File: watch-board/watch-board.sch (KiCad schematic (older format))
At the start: 41 parts

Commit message: finished LTC3531-3 design
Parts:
- removed BT?: BAT_ML2020, symbol luke:BAT_ML2020
- removed C?: C_10uF, Capacitor_SMD:C_0805_2012Metric, symbol luke:C_10uF
- removed C? (x2): C_1uF, footprints:C_0805_OEM, symbol formula:C_1uF
- removed R? (x2): R_1M, Resistor_SMD:R_0805_2012Metric, symbol luke:R_1M
- removed R?: R_475K, Resistor_SMD:R_0805_2012Metric, symbol luke:R_475K
- removed R?: R_2K, Resistor_SMD:R_0805_2012Metric, symbol luke:R_2K
- removed R?: R_165K, Resistor_SMD:R_0805_2012Metric, symbol luke:R_165K
- removed R?: R_499K, Resistor_SMD:R_0805_2012Metric, symbol luke:R_499K
- removed R?: R_160, Resistor_SMD:R_0805_2012Metric, symbol luke:R_160
- removed SC?: Solar-Cells_KXOB25-05X3F, symbol luke:Solar-Cells_KXOB25-05X3F
- removed U?: Regulator_LTC3105, Digikey-footprints:MSOP-12-1EP_W3mm, symbol luke:Regulator_LTC3105
- added BT?: BAT_ML2020, symbol luke:BAT_ML2020
- added C?: C_10uF, Capacitor_SMD:C_0805_2012Metric, symbol luke:C_10uF
- added C?: C_2.2uF, Capacitor_SMD:C_0805_2012Metric, symbol luke:C_2.2uF
- added L?: L_22uH, Inductor_SMD:L_Wuerth_WE-TPC-3816, symbol luke:L_22uH
- added L?: L_10uH, Inductor_SMD:L_1812_4532Metric, symbol luke:L_10uH
- added SC?: Solar-Cells_KXOB25-05X3F, symbol luke:Solar-Cells_KXOB25-05X3F
- added U?: Regulator_BQ25504, Package_DFN_QFN:QFN-16-1EP_3x3mm_P0.5mm_EP1.8x1.8mm, symbol luke:Regulator_BQ25504
- added U?: Regulator_LTC3531-3, Package_TO_SOT_SMD:TSOT-23-6, symbol luke:Regulator_LTC3531-3
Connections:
- wire segments 121 -> 118

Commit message: finished REV1 of board
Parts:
- removed BT? (x2): BAT_ML2020, symbol luke:BAT_ML2020
- removed C?: C_4.7uF, Capacitor_SMD:C_1206_3216Metric, symbol luke:C_4.7uF
- removed C?: C_7pF, Capacitor_SMD:C_0805_2012Metric, symbol luke:C_7pF
- removed C?: C_1uF, Capacitor_SMD:C_0805_2012Metric, symbol luke:C_1uF
- removed C?: C_0.1uF, Capacitor_SMD:C_0805_2012Metric, symbol luke:C_0.1uF
- removed D? (x3): D-Schotkey_BAT54HT1G, Diode_SMD:D_SOD-323, symbol luke:D-Schotkey_BAT54HT1G
- removed Q?: Transistor_FZT796ATA, Package_TO_SOT_SMD:SOT-223, symbol luke:Transistor_FZT796ATA
- removed R?: R_51.1K, Resistor_SMD:R_0805_2012Metric, symbol luke:R_51.1K
- removed R?: R_78.7K, Resistor_SMD:R_0805_2012Metric, symbol luke:R_78.7K
- removed R?: R_160, Resistor_SMD:R_0805_2012Metric, symbol luke:R_160
- removed R?: R_100K, Resistor_SMD:R_0805_2012Metric, symbol luke:R_100K
- removed R?: R_200K, Resistor_SMD:R_0805_2012Metric, symbol luke:R_200K
- removed R?: R_1.2M, Resistor_SMD:R_0805_2012Metric, symbol luke:R_1.2M
- removed R?: R_49.9K, Resistor_SMD:R_0805_2012Metric, symbol luke:R_49.9K
- removed SC?: Solar-Cells_KXOB25-02X8F, symbol luke:Solar-Cells_KXOB25-02X8F
- removed U?: Comparitor_TPS3700DDCR, digikey-footprints:SOT-23-6, symbol luke:Comparitor_TPS3700DDCR
- removed U?: Regulator_LP2980-ADJ, Package_TO_SOT_SMD:SOT-23-5, symbol luke:Regulator_LP2980-ADJ
- added BT1: BAT_ML1220, Battery:Battery_Panasonic_CR1220-VCN_Vertical_CircularHoles, symbol luke:BAT_ML1220
- added C10: C_2.2uF, Capacitor_SMD:C_0805_2012Metric, symbol luke:C_2.2uF
- added C11, C17: C_0.1uF, Capacitor_SMD:C_0805_2012Metric, symbol luke:C_0.1uF
- added C13: C_0.01uF, Capacitor_SMD:C_0805_2012Metric, symbol luke:C_0.01uF
- added C14, C16: C_4.7uF, Capacitor_SMD:C_0805_2012Metric, symbol luke:C_4.7uF
- added C7, C9: C_20pF, Capacitor_SMD:C_0805_2012Metric, symbol luke:C_20pF
- added D1: D-Schotkey_BAT54HT1G, Diode_SMD:D_SOD-323, symbol luke:D-Schotkey_BAT54HT1G
- added J2: Conn_02x05, Connector_PinSocket_2.54mm:PinSocket_2x05_P2.54mm_Vertical, symbol luke:Conn_02x05
- added J3: FPC-Conn_01x08, luke-footprints:Connector_Molex-5014610891, symbol luke:FPC-Conn_01x08
- added R1: R_330, footprints:R_0805_OEM, symbol luke:R_330
- added R10, R7: R_4.22M, Resistor_SMD:R_0805_2012Metric, symbol luke:R_4.22M
- added R11: R_5.11M, Resistor_SMD:R_0805_2012Metric, symbol luke:R_5.11M
- added R12: R_6.04M, Resistor_SMD:R_0805_2012Metric, symbol luke:R_6.04M
- added R13: R_10M, Resistor_SMD:R_0805_2012Metric, symbol luke:R_10M
- added R14: R_3.83M, Resistor_SMD:R_0805_2012Metric, symbol luke:R_3.83M
- added R2: R_220K, Resistor_SMD:R_0805_2012Metric, symbol luke:R_220K
- added R3, R4: R_10K, Resistor_SMD:R_0805_2012Metric, symbol luke:R_10K
- added R5: R_3.74M, Resistor_SMD:R_0805_2012Metric, symbol luke:R_3.74M
- added R6: R_6.19M, Resistor_SMD:R_0805_2012Metric, symbol luke:R_6.19M
- added R8: R_5.62M, Resistor_SMD:R_0805_2012Metric, symbol luke:R_5.62M
- added R9: R_806K, Resistor_SMD:R_0805_2012Metric, symbol luke:R_806K
- added S1: Switch_1767, Connector_PinSocket_2.54mm:PinSocket_1x02_P2.54mm_Vertical, symbol luke:Switch_1767
- added XTAL1: Crystals_32.768-SMD, Digikey-footprints:SMD-2_3.2x1.5mm, symbol luke:Crystals_32.768-SMD
- C1, C3, C5, C8: renamed from C?; Digi-Key_PN 399-1177-1-ND -> 399-8000-1-ND; Purchasing Link https://www.digikey.com/product-detail/en/kemet/C0805C104Z5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 -> https://www.digikey.com/product-detail/en/kemet/C0805C104M3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
- L1: renamed from L?; Purchasing Link (none) -> https://www.digikey.com/product-detail/en/murata-electronic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
- L2: renamed from L?; Purchasing Link (none) -> https://www.digikey.com/product-detail/en/w%C3%BCrth-elektr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; PurchasingLink https://www.digikey.com/product-detail/en/w%C3%BCrth-elektr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 -> (none)
- SC1: renamed from SC?; footprint (none) -> luke-footprints:Solar-Cells_KXOB25
- U3: renamed from U?; footprint Package_DFN_QFN:QFN-16-1EP_3x3mm_P0.5mm_EP1.8x1.8mm -> Package_DFN_QFN:VQFN-16-1EP_3x3mm_P0.5mm_EP1.8x1.8mm_ThermalVias
- gave numbers to parts that had none: 8
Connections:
- net labels added: BUTTON, DISP, EXTCOMIN, LOAD, MISO, MOSI, NSS, OK_HYST, OK_PROG, PA2, PA3, SCK, VBAT_OK, VBAT_OV, VBAT_UV
- net labels removed: VCC, V_BAT, V_Charge, V_Charge_ON
- wire segments 118 -> 140
- no-connect marks 0 -> 14
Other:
- note added: "Buck/Boost Converter"
- note added: "Connectors"
- note added: "Engery Harvesting"
- note added: "LCD Connector"
- note added: "R_OC"
- note added: "R_OK"
- note added: "R_OV"
- note added: "R_UV"
- note added: "STM32"
- note added: "Shake Switch"
- note removed: "Calcular ESR is 886Ohms\n160Ohm resistor used for current limiting durring charging"
- note removed: "Rt = 1500000 (high value for low current draw)\nR3 = (Rt/Vo)*Vi\nR2 = ((Rt/Vu)*(Vi-Vhys))-R3\nR1 = Rt - R2 - R3\nVi = 0.4V\nVo = 3V\nVu = 2V\nVhys = 5.5mV [(Vi+) - (Vi-)]\n\nR2 =95875 (rounding up to 100K for convience)\nR3 = 200K"
- note removed: "TODO: Add SPI Pins"
- note removed: "Vout = Vref + (Vref * (Radj/51.1K))\nVref Typical = 1.225 (min = 1.213 max = 1.237)\nRadj = 78.7K\nVout =3.11\n3.08 < Vout < 3.14"
- note removed: "use BUCK-BOOST (TPS6305) to set VDD to 3V"
- moved on the sheet: C1, C12, C15, C2, C3, C4, C5, C6, C8, J1, L1, L2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

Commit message: Schematic for Version 2
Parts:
- removed C15: C_10uF, Capacitor_SMD:C_0805_2012Metric, symbol luke:C_10uF
- removed L1: L_10uH, Inductor_SMD:L_1812_4532Metric, symbol luke:L_10uH
- removed R1: R_330, footprints:R_0805_OEM, symbol luke:R_330
- removed R10, R7: R_4.22M, Resistor_SMD:R_0805_2012Metric, symbol luke:R_4.22M
- removed R11: R_5.11M, Resistor_SMD:R_0805_2012Metric, symbol luke:R_5.11M
- removed R12: R_6.04M, Resistor_SMD:R_0805_2012Metric, symbol luke:R_6.04M
- removed R13: R_10M, Resistor_SMD:R_0805_2012Metric, symbol luke:R_10M
- removed R14: R_3.83M, Resistor_SMD:R_0805_2012Metric, symbol luke:R_3.83M
- removed R5: R_3.74M, Resistor_SMD:R_0805_2012Metric, symbol luke:R_3.74M
- removed R6: R_6.19M, Resistor_SMD:R_0805_2012Metric, symbol luke:R_6.19M
- removed U3: Regulator_BQ25504, Package_DFN_QFN:VQFN-16-1EP_3x3mm_P0.5mm_EP1.8x1.8mm_ThermalVias, symbol luke:Regulator_BQ25504
- added C33: C_10uF, Capacitor_SMD:C_0805_2012Metric, symbol luke:C_10uF
- added L3: L_10uH, Inductor_SMD:L_1812_4532Metric, symbol luke:L_10uH
- added R13: R_330, footprints:R_0805_OEM, symbol luke:R_330
- added R17: R_3.74M, Resistor_SMD:R_0805_2012Metric, symbol luke:R_3.74M
- added R18: R_6.19M, Resistor_SMD:R_0805_2012Metric, symbol luke:R_6.19M
- added R19, R22: R_4.22M, Resistor_SMD:R_0805_2012Metric, symbol luke:R_4.22M
- added R23: R_5.11M, Resistor_SMD:R_0805_2012Metric, symbol luke:R_5.11M
- added R24: R_6.04M, Resistor_SMD:R_0805_2012Metric, symbol luke:R_6.04M
- added R25: R_10M, Resistor_SMD:R_0805_2012Metric, symbol luke:R_10M
- added R26: R_3.83M, Resistor_SMD:R_0805_2012Metric, symbol luke:R_3.83M
- added U11: Regulator_BQ25504, Package_DFN_QFN:VQFN-16-1EP_3x3mm_P0.5mm_EP1.8x1.8mm_ThermalVias, symbol luke:Regulator_BQ25504
- renumbered BT1 to BT2, C1 to C19, C2 to C20, C3 to C21, C4 to C22, C5 to C23, C6 to C24, C7 to C25, C8 to C26, C9 to C27, C10 to C28, C11 to C29, C12 to C30, C13 to C31, C14 to C32, C16 to C34, C17 to C35, D1 to D2, J1 to J2, J2 to J3, J3 to J4, L2 to L4, R2 to R14, R3 to R15, R4 to R16, R8 to R20, R9 to R21, S1 to S3, SC1 to SC2, U2 to U10, U1 to U9, XTAL1 to XTAL2

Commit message: Stopping work on Watch-V2. Changing driver & Display on Watch-V1.
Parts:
- removed C28: C_2.2uF, Capacitor_SMD:C_0805_2012Metric, symbol luke:C_2.2uF
- removed C29: C_0.1uF, Capacitor_SMD:C_0805_2012Metric, symbol luke:C_0.1uF
- removed J3: Conn_02x05, Connector_PinSocket_2.54mm:PinSocket_2x05_P2.54mm_Vertical, symbol luke:Conn_02x05
- removed J4: FPC-Conn_01x08, luke-footprints:Connector_Molex-5014610891, symbol luke:FPC-Conn_01x08
- removed R15, R16: R_10K, Resistor_SMD:R_0805_2012Metric, symbol luke:R_10K
- removed U9: MCU_STM32L051K8Tx, Package_QFP:LQFP-32_7x7mm_P0.8mm, symbol luke:MCU_STM32L051K8Tx
- added BZ1: Buzzer_PB9.9-3V, symbol luke:Buzzer_PB9.9-3V
- added C10, C11, C12, C15: C_0.1uF, Capacitor_SMD:C_0805_2012Metric, symbol luke:C_0.1uF
- added C13: C_22uF, Capacitor_SMD:C_0805_2012Metric, symbol luke:C_22uF
- added C14: C_10uF, Capacitor_SMD:C_0805_2012Metric, symbol luke:C_10uF
- added R1, R2: R_4.7K, Resistor_SMD:R_0805_2012Metric, symbol luke:R_4.7K
- added R3: R_330, footprints:R_0805_OEM, symbol luke:R_330
- added R8: R_49.9K, Resistor_SMD:R_0805_2012Metric, symbol luke:R_49.9K
- added U1: LCD_OD-204, luke-footprints:LCD_OD-204, symbol luke:LCD_OD-204
- added U2: Display-Driver_PCA8561ANH, Package_DFN_QFN:QFN-32-1EP_5x5mm_P0.5mm_EP3.6x3.6mm, symbol luke:Display-Driver_PCA8561ANH
- added U3: MCU_STM32L051K8Ux, Package_DFN_QFN:QFN-32-1EP_5x5mm_P0.5mm_EP3.3x3.3mm, symbol luke:MCU_STM32L051K8Ux
- added U4: Sensor_VCNL4010, luke-footprints:Sensor_VCNL4010, symbol luke:Sensor_VCNL4010
- BT1: renamed from BT2; footprint Battery:Battery_Panasonic_CR1220-VCN_Vertical_CircularHoles -> luke-footprints:BAT_ML1220-F1A; Purchasing Link https://www.digikey.com/product-detail/en/panasonic-bsg/ML-1220-F1BN/P663-ND/2404068 -> https://www.digikey.com/product-detail/en/panasonic-bsg/ML-1220-F1AN/P295-ND/447504
- renumbered C19 to C1, C31 to C16, C32 to C17, C30 to C18, C33 to C19, C20 to C2, C34 to C20, C35 to C21, C21 to C3, C22 to C4, C23 to C5, C24 to C6, C25 to C7, C26 to C8, C27 to C9, D2 to D1, J2 to J1, L4 to L1, L3 to L2, R18 to R10, R19 to R11, R20 to R12, R21 to R13, R22 to R14, R23 to R15, R24 to R16, R25 to R17, R26 to R18, R13 to R4, R14 to R5, R17 to R9, S3 to S1, SC2 to SC1, U11 to U5, U10 to U6, XTAL2 to XTAL1
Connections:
- net labels added: 1A, 1B, 1C, 1D, 1E, 1F, 1G, 2A, 2B, 2C, 2D, 2E, 2F, 2G, BUZZER, COM1, COM2, INT, RESET, SCL, SDA, VCC
- net labels removed: EXTCOMIN, MISO, MOSI, NSS, PA2, PA3, SCK
- wire segments 140 -> 191
- no-connect marks 14 -> 25
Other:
- note added: "Conn"
- note added: "Display & Driver"
- note removed: "Connectors"
- note removed: "LCD Connector"
- moved on the sheet: BT1, C1, C16, C17, C18, C19, C2, C20, C21, C3, C4, C5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

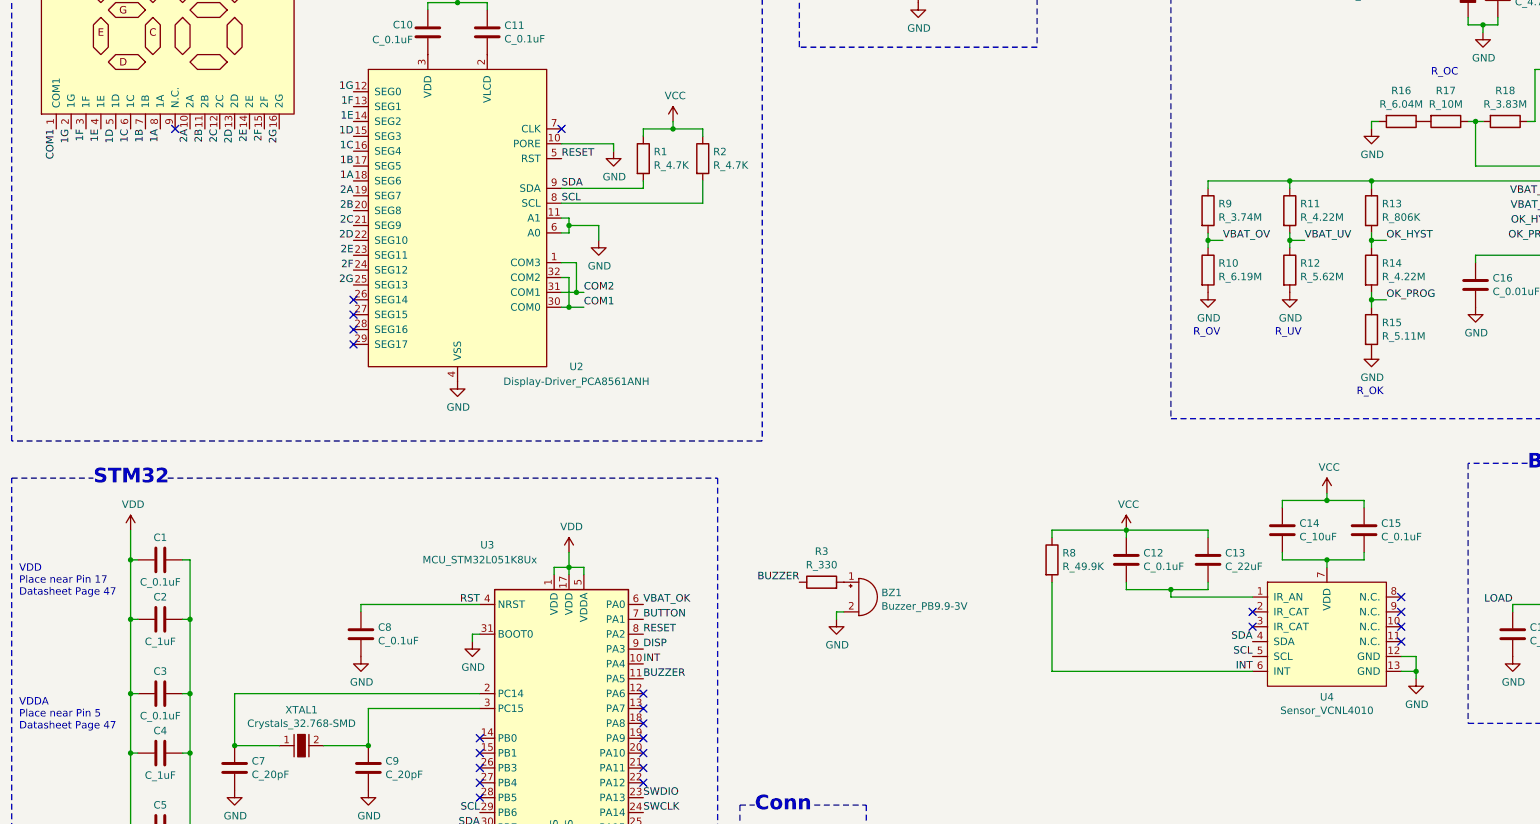
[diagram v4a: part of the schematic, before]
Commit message: Adding Phototransistors for Gesture Sensing
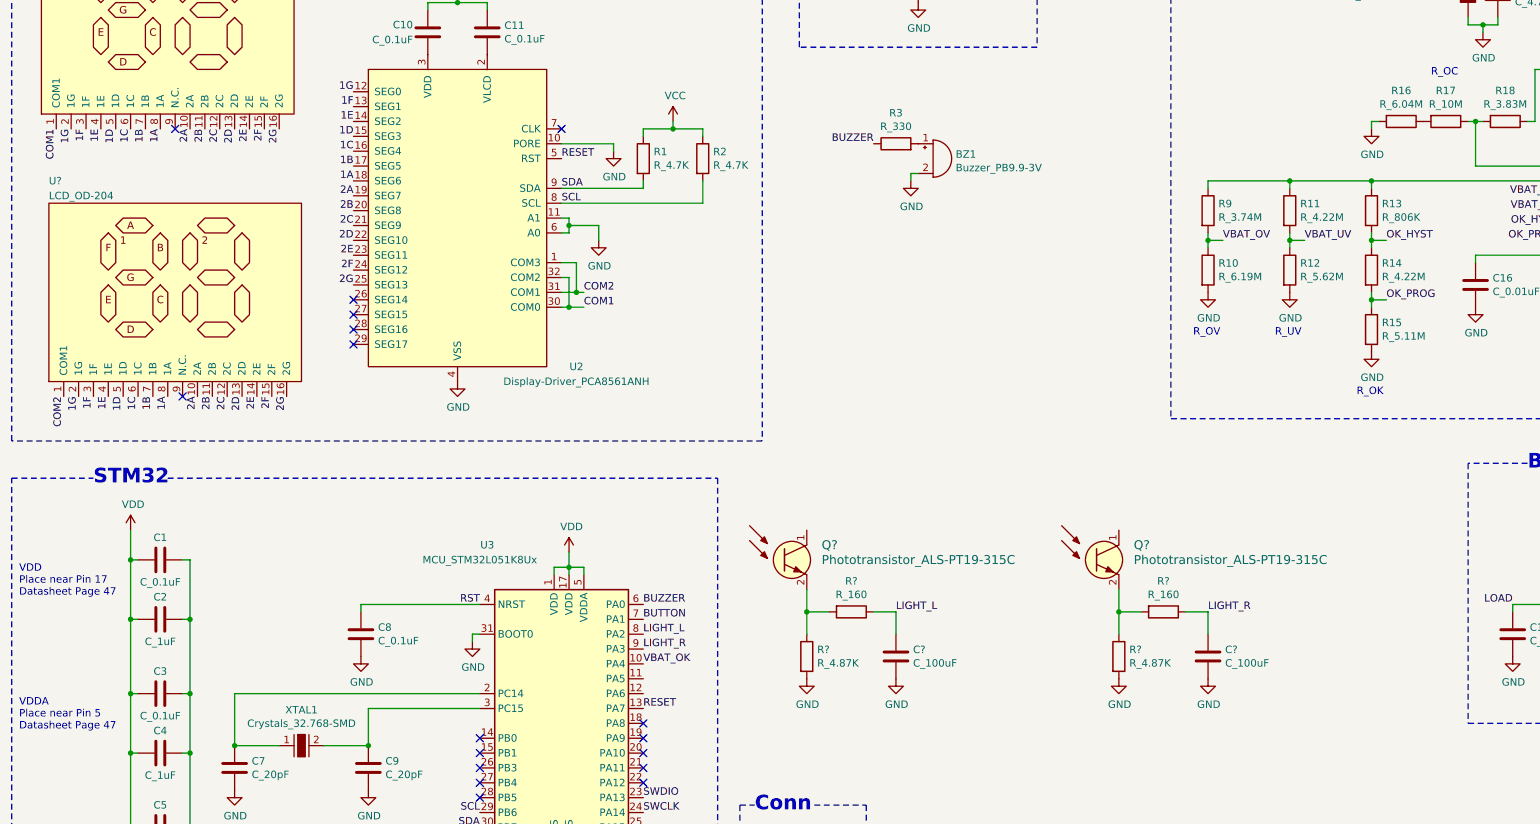
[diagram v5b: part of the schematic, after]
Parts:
- removed C12, C15: C_0.1uF, Capacitor_SMD:C_0805_2012Metric, symbol luke:C_0.1uF
- removed C13: C_22uF, Capacitor_SMD:C_0805_2012Metric, symbol luke:C_22uF
- removed C14: C_10uF, Capacitor_SMD:C_0805_2012Metric, symbol luke:C_10uF
- removed R8: R_49.9K, Resistor_SMD:R_0805_2012Metric, symbol luke:R_49.9K
- removed U4: Sensor_VCNL4010, luke-footprints:Sensor_VCNL4010, symbol luke:Sensor_VCNL4010
- added C? (x2): C_100uF, Capacitor_SMD:C_0805_2012Metric, symbol luke:C_100uF
- added Q? (x2): Phototransistor_ALS-PT19-315C, digikey-footprints:LED_2-SMD_No_Lead_1.7x0.8mm, symbol luke:Phototransistor_ALS-PT19-315C
- added R? (x2): R_4.87K, Resistor_SMD:R_0805_2012Metric, symbol luke:R_4.87K
- added R? (x2): R_160, Resistor_SMD:R_0805_2012Metric, symbol luke:R_160
- added U?: LCD_OD-204, luke-footprints:LCD_OD-204, symbol luke:LCD_OD-204
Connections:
- net INT is gone; now on net VBAT_OK: U3.10 (PA4)
- net 1A: now also U?.8 (1A)
- net 1B: now also U?.7 (1B)
- net 1C: now also U?.6 (1C)
- net 1D: now also U?.5 (1D)
- net 1E: now also U?.4 (1E)
- net 1F: now also U?.3 (1F)
- net 1G: now also U?.2 (1G)
- net 2A: now also U?.10 (2A)
- net 2B: now also U?.11 (2B)
- net 2C: now also U?.12 (2C)
- net 2D: now also U?.13 (2D)
- net 2E: now also U?.14 (2E)
- net 2F: now also U?.15 (2F)
- net 2G: now also U?.16 (2G)
- net BUZZER: now also U3.6 (PA0); no longer U3.11 (PA5)
- net COM2: now also U?.1 (COM1)
- net GND: now also C?.2, C?.2, R?.2, R?.2
- net RESET: now also U3.13 (PA7); no longer U3.8 (PA2)
- net VBAT_OK: no longer U3.6 (PA0)
- net DISP renamed LIGHT_R
- net LIGHT_R: now also C?.1, R?.1
- new net: Q?.2 (E), R?.1, R?.2 (x2)
- new net LIGHT_L: C?.1, R?.1, U3.8 (PA2)
- no-connect marks 25 -> 18
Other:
- moved on the sheet: BZ1, R3

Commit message: design complete TODO: add justifications for component choice
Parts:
- removed BZ1: Buzzer_PB9.9-3V, symbol luke:Buzzer_PB9.9-3V
- removed R3, R4: R_330, footprints:R_0805_OEM, symbol luke:R_330
- added BZ?: Buzzer_Piezo-35mm, Connector_PinSocket_2.54mm:PinSocket_1x02_P2.54mm_Vertical, symbol luke:Buzzer_Piezo-35mm
- added D?: D-Schotkey_BAT54HT1G, Diode_SMD:D_SOD-323, symbol luke:D-Schotkey_BAT54HT1G
- added D?: LED_IN-S63AT5UW, Connector_Wire:SolderWire-0.5sqmm_1x02_P4.8mm_D0.9mm_OD2.3mm, symbol luke:LED_IN-S63AT5UW
- added Q?: Transistor_MMBT3904-TP, Package_TO_SOT_SMD:SOT-23, symbol luke:Transistor_MMBT3904-TP
- added R? (x2): R_604, Resistor_SMD:R_0805_2012Metric, symbol luke:R_604
- added R?: R_10K, Resistor_SMD:R_0805_2012Metric, symbol luke:R_10K
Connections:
- net BUTTON: now also R?.2
- net BUZZER: now also R?.2
- net GND: now also D?.1 (K), Q?.2 (E)
- net RESET: now also U3.18 (PA8); no longer U3.13 (PA7)
- net VCC: now also BZ?.1 (-), D?.1 (K)
- net at R5.1, S1.1: now also R?.1
- net VLIGHT_L: now reaches U3.11 (PA5)
- net VLIGHT_L: now also Q?.1 (C)
- net VLIGHT_R: now reaches U3.12 (PA6)
- net VLIGHT_R: now also Q?.1 (C)
- new net: BZ?.2 (+), D?.2 (A), Q?.3 (C)
- new net: Q?.1 (B), R?.1
- new net: D?.2 (A), R?.2
- new net LIGHT: R?.1, U3.13 (PA7)
- no-connect marks 18 -> 17
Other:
- note added: "Buzzer"
- note added: "Light"
- note added: "Light Sensors"
- moved on the sheet: BT, C, D, J, L, Q, R, S, SC, U

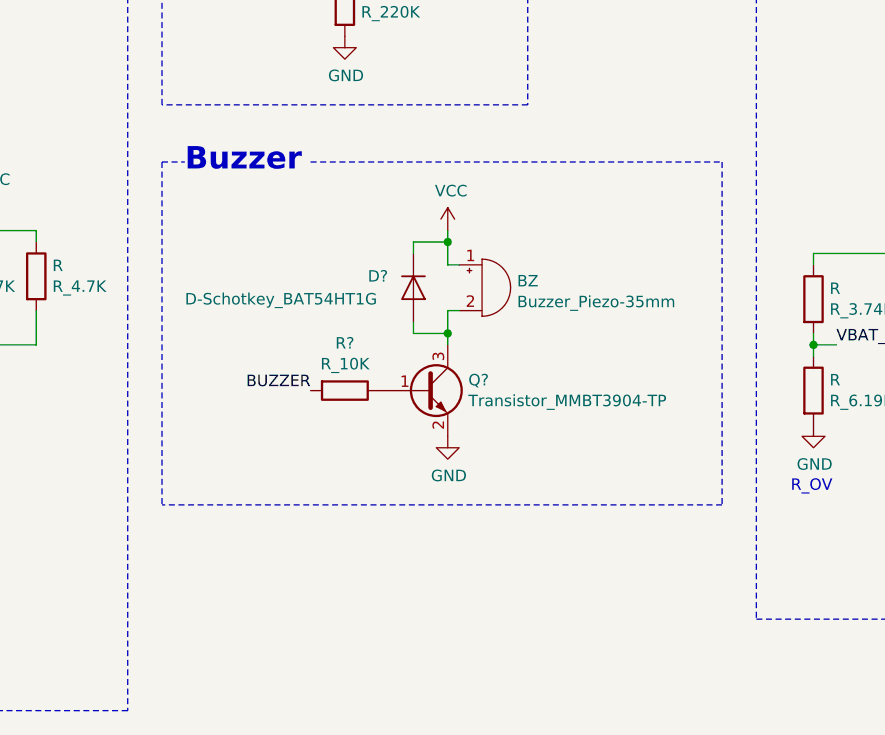
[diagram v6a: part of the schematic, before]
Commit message: adding current limiting resistor to buzzer
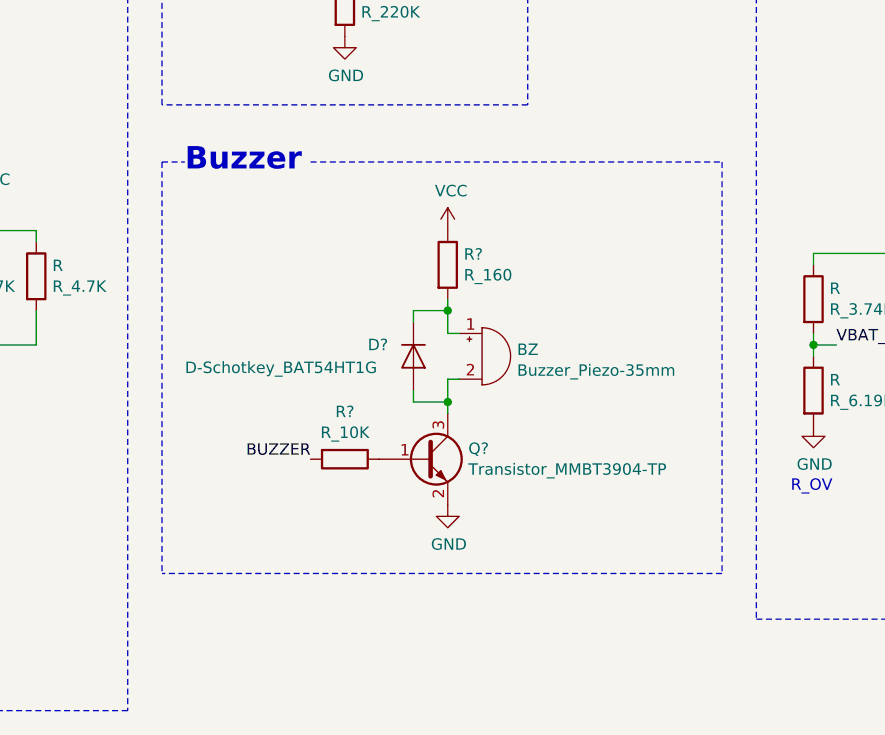
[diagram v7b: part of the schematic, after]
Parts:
- added R?: R_160, Resistor_SMD:R_0805_2012Metric, symbol luke:R_160
- gave numbers to parts that had none: 5
- renumbered BT1 to BT, C3 to C, C5 to C, C1 to C, C4 to C, C6 to C, C18 to C, C2 to C, C9 to C, C7 to C, C8 to C, C16 to C, C17 to C, C20 to C, C21 to C, C19 to C, C10 to C, C11 to C, D1 to D, U1 to DS, J1 to J, L1 to L, L2 to L, R13 to R, R12 to R, R5 to R, R18 to R, R17 to R, R16 to R, R15 to R, R14 to R, R10 to R, R9 to R, R11 to R, R1 to R, R2 to R, S1 to S, SC1 to SC, U6 to U, U3 to U, U5 to U, U2 to U, XTAL1 to XTAL
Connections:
- net VCC: now also R?.1; no longer BZ.1 (-), D?.1 (K)
- new net: BZ.1 (-), D?.1 (K), R?.2
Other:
- moved on the sheet: BZ, D?, Q?, R?
